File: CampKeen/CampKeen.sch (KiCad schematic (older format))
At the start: 65 parts, among them IC1 LM2597MX-ADJ_NOPB, IC2 LM2670SX-5.0_NOPB, IC3 DS3231SN#, IC4 CD74HC4050ME4, IC5 OPA2340PA, J1 Vin, J2 CircuitSetupsSplitPhase, J3 Vin, J4 Screw_Terminal_01x04, J5 GenEnclosure, J6 GenHeadL, J7 GenHeadR, J8 Conn_01x02, P1 Power, P10 CONN_01X01, P11 CONN_01X01, P12 CONN_01X01, P13 CONN_01X01, P2 Analog, P3 Analog, P4 Digital, P5 PWM, P6 PWM, P7 Communication, P8 CONN_01X01, P9 CONN_01X01, Q40 IRF9Z34NPBF, U2 MAX232

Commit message: updated the pin mapping to the terms. cleaned up the Schematic. PCB placement and routing is what is left to do.
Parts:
- removed J4: Screw_Terminal_01x04, TerminalBlock_TE-Connectivity:TerminalBlock_TE_282834-4_1x04_P2.54mm_Horizontal, symbol Connector:Screw_Terminal_01x04
- added 5VOut1: VS, SamacSys_Parts:BK_HTC-15M, symbol SamacSys_Parts:BK_HTC-15M
- added D3: LED, symbol Device:LED
- added IC6: OPA2340PA, SamacSys_Parts:DIP794W53P254L959H508Q8N, symbol SamacSys_Parts:OPA2340PA
- added J8, J9: Conn_01x02, Connector_PinHeader_2.54mm:PinHeader_1x02_P2.54mm_Vertical, symbol Connector_Generic:Conn_01x02
- added R112, R113: 47K, Resistor_THT:R_Axial_DIN0207_L6.3mm_D2.5mm_P2.54mm_Vertical, symbol Device:R
- added R117: 330, Resistor_THT:R_Axial_DIN0207_L6.3mm_D2.5mm_P2.54mm_Vertical, symbol Device:R
- added RV2, RV3: 500k, Potentiometer_THT:Potentiometer_Bourns_3296W_Vertical, symbol Device:R_POT_US
- IC4: renamed from IC5; footprint DIP794W53P254L959H508Q8N -> SamacSys_Parts:DIP794W53P254L959H508Q8N
- IC5: renamed from IC4; footprint SOIC127P600X175-16N -> SamacSys_Parts:SOIC127P600X175-16N
- IO1: renamed from Tanks0; value Tanks -> IO1
- IO2: renamed from I1; value I1 -> IO2
- IO3: renamed from O1; value O1 -> IO3
- IO4: renamed from IO1; value IO2 -> IO4
- RV1: value R_POT_US -> 500k
- renumbered C7 to C10, C5 to C11, C14 to C12, C15 to C13, C16 to C14, C17 to C15, C9 to C3, C18 to C4, C3 to C5, C8 to C6, C4 to C7, C6 to C8, C10 to C9, J3 to J2, J8 to J3, J2 to J4, L2 to L1, L1 to L2, Q40 to Q1, R6 to R10, R29 to R11, R89 to R5, R28 to R6, R82 to R7, R35 to R8, R5 to R9, U2 to U1
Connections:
- net labels added: AUXVoltage1, AUXVoltage2, AlarmTTL, BRLED, BathRoomTTL, COMRXTTL, COMTXTTL, CWV, DisplayLED, ENLCD, EnCS, IO11, IO110, IO111, IO112, IO12, IO13, IO14, IO15, IO16, IO17, IO18, IO19, IO210, IO211, IO212, IO22, IO23, IO24, IO25, IO26, IO27, IO28, IO29, IO31, IO311, IO32, IO33, IO34, IO35, IO38, IO41, IO410, IO411, IO412, IO42, IO44, IO45, IO47, IO48, IO49, KLED, KitchenTTL, LCBBACK, LCDBL, LCDPOWER, RTankPOWER, RX232, SO1, SO2, SO3, SO4, SO5, SPIn1, SPIn2, SPIn3, SPIn4, SPIn5, SPIn6, SpareTTL, TX232, WLED, WP, WPS, WSS, WSiren
- wire segments 305 -> 447
- no-connect marks 38 -> 39
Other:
- note added: "Energy Monitoring"
- note added: "IO Terminals"
- note added: "Temps: RTD and NTC"
- note removed: "RTD DEV"
- moved on the sheet: C11, C3, C4, C5, C6, C9, D1, IC2, IC3, IC5, IO1, IO2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

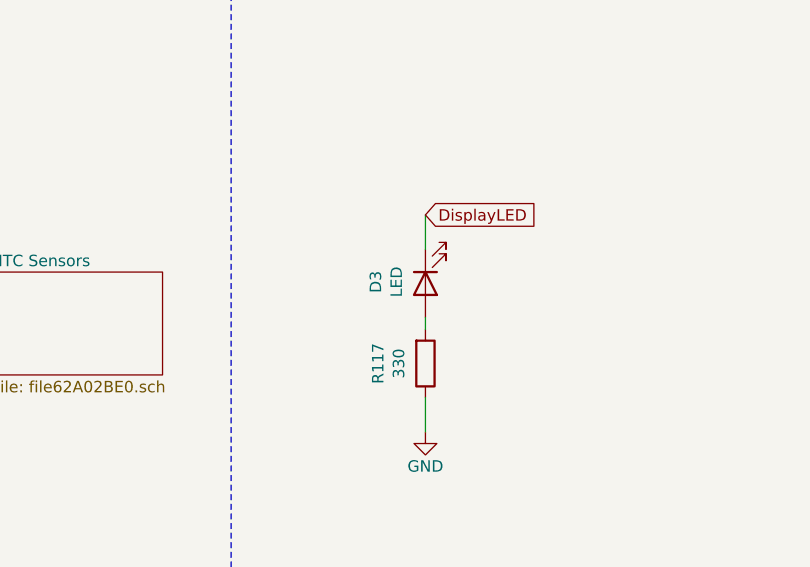
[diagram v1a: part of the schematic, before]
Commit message: fixed the Diode orientation.
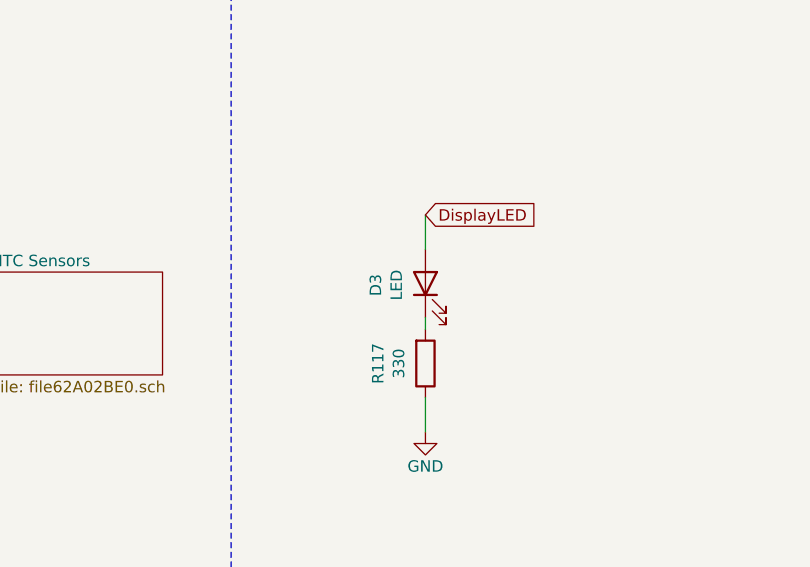
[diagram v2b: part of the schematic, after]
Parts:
- D3: footprint (none) -> LED_THT:LED_D3.0mm
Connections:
- net DisplayLED: now also D3.2 (A); no longer D3.1 (K)
- net at R117.2: now also D3.1 (K); no longer D3.2 (A)
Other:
- moved on the sheet: D3
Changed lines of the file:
@@
 Wire Wire Line
 	17800 2600 17800 2750
-$Comp
-L Device:LED D3
-U 1 1 648097C3
-P 17800 2100
-F 0 "D3" H 17793 2317 50  0000 C CNN
-F 1 "LED" H 17793 2226 50  0000 C CNN
-F 2 "" H 17800 2100 50  0001 C CNN
-F 3 "~" H 17800 2100 50  0001 C CNN
-	1    17800 2100
-	0    -1   1    0
-$EndComp
 Wire Wire Line
 	17800 2300 17800 2250
-Wire Wire Line
-	17800 1950 17800 1800
 NoConn ~ 21800 1300
 NoConn ~ 21800 1200
@@
 Wire Wire Line
 	6900 7750 7450 7750
+Wire Wire Line
+	17800 1950 17800 1800
+$Comp
+L Device:LED D3
+U 1 1 648097C3
+P 17800 2100
+F 0 "D3" H 17793 2317 50  0000 C CNN
+F 1 "LED" H 17793 2226 50  0000 C CNN
+F 2 "LED_THT:LED_D3.0mm" H 17800 2100 50  0001 C CNN
+F 3 "~" H 17800 2100 50  0001 C CNN
+	1    17800 2100
+	0    -1   -1   0
+$EndComp
 $EndSCHEMATC

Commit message: separated the 12 and 5 volt outputs. added another spare output.
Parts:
- removed J2: Vin, TerminalBlock_Phoenix:TerminalBlock_Phoenix_MKDS-1,5-2-5.08_1x02_P5.08mm_Horizontal, symbol Connector:Screw_Terminal_01x02
- added J2: Screw_Terminal_01x03, TerminalBlock_Phoenix:TerminalBlock_Phoenix_MKDS-1,5-3-5.08_1x03_P5.08mm_Horizontal, symbol Connector:Screw_Terminal_01x03
- renumbered C9 to C10, C10 to C11, C11 to C3, C3 to C4, C4 to C5, C5 to C6, C6 to C7, C7 to C8, C8 to C9, IC5 to IC1, IC1 to IC2, IC2 to IC3, IC3 to IC4, IC4 to IC5, J4 to J3, J8 to J4, J3 to J5, J9 to J6, J5 to J7, J6 to J8, J7 to J9, R8 to R10, R112 to R11, R11 to R12, R113 to R13, R117 to R14, R9 to R6, R10 to R7, R6 to R8, R7 to R9, RV2 to RV1, RV1 to RV2
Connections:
- net +12V: now also J2.1 (Pin_1)
- net GND: now also J2.2 (Pin_2)
- net 15(Rx3) renamed SO6
- new net SpareOut6: J2.3 (Pin_3)
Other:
- note added: "Inputs"
- note added: "Outputs"
- note added: "Tank Sensors"
- moved on the sheet: D3, R14

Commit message: fixing the powered 12v out and moving it on the other side of the reverse polarity protection for everything else. Added a Reverse polarity protection diode (3A Schottkey). Also this is still behind the main protection fuse.
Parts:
- added D4: SR305-TP, DIOAD2860W130L840D505, symbol SamacSys_Parts:SR305-TP
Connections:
- net +12V: no longer J2.1 (Pin_1)
- net at Main1.2, Q1.2: now also D4.1
- new net: D4.2, J2.1 (Pin_1)
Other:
- moved on the sheet: D3, J2, R14
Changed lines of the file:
@@
 Text Label 21800 1400 0    60   ~ 0
 AREF
-Text Notes 20075 575  0    60   ~ 0
+Text Notes 19225 575  0    60   ~ 0
 Shield for Arduino Mega Rev 3
 Text Notes 22400 1000 0    60   ~ 0
@@
 	22900 1000 22150 1000
 Wire Notes Line
-	21550 650  21550 475
+	20700 650  20700 475
 Wire Notes Line
-	20050 650  21550 650
+	19200 650  20700 650
 Wire Wire Line
 	20400 1100 20400 1800
@@
 $EndComp
 Wire Wire Line
-	3450 1100 3200 1100
-Wire Wire Line
 	4050 1100 4750 1100
 $Comp
@@
 Wire Wire Line
 	4750 1100 4750 1050
-Wire Wire Line
-	2400 1100 1650 1100
 Connection ~ 2400 1100
 $Comp
@@
 	900  10200 900  11000
 Wire Wire Line
-	4600 1200 4600 1250
+	4350 2500 4350 2550
 Wire Wire Line
-	4750 1200 4600 1200
+	4500 2500 4350 2500
 $Comp
 L power:GND #PWR027
 U 1 1 61491D30
-P 4600 1250
-F 0 "#PWR027" H 4600 1000 50  0001 C CNN
-F 1 "GND" H 4605 1077 50  0000 C CNN
-F 2 "" H 4600 1250 50  0001 C CNN
-F 3 "" H 4600 1250 50  0001 C CNN
-	1    4600 1250
+P 4350 2550
+F 0 "#PWR027" H 4350 2300 50  0001 C CNN
+F 1 "GND" H 4355 2377 50  0000 C CNN
+F 2 "" H 4350 2550 50  0001 C CNN
+F 3 "" H 4350 2550 50  0001 C CNN
+	1    4350 2550
 	1    0    0    -1
 $EndComp
@@
 Wire Wire Line
 	21550 1600 22200 1600
-Text GLabel 17900 1550 2    50   Input ~ 0
+Text GLabel 18000 750  2    50   Input ~ 0
 DisplayLED
 $Comp
 L Device:R R14
 U 1 1 647E4AAA
-P 17900 2200
-F 0 "R14" V 17693 2200 50  0000 C CNN
-F 1 "330" V 17784 2200 50  0000 C CNN
-F 2 "Resistor_THT:R_Axial_DIN0207_L6.3mm_D2.5mm_P2.54mm_Vertical" V 17830 2200 50  0001 C CNN
-F 3 "~" H 17900 2200 50  0001 C CNN
-	1    17900 2200
+P 18000 1400
+F 0 "R14" V 17793 1400 50  0000 C CNN
+F 1 "330" V 17884 1400 50  0000 C CNN
+F 2 "Resistor_THT:R_Axial_DIN0207_L6.3mm_D2.5mm_P2.54mm_Vertical" V 17930 1400 50  0001 C CNN
+F 3 "~" H 18000 1400 50  0001 C CNN
+	1    18000 1400
 	1    0    0    1
 $EndComp
@@
 L power:GND #PWR056
 U 1 1 647E4AB0
-P 17900 2500
-F 0 "#PWR056" H 17900 2250 50  0001 C CNN
-F 1 "GND" H 17900 2350 50  0000 C CNN
-F 2 "" H 17900 2500 50  0000 C CNN
-F 3 "" H 17900 2500 50  0000 C CNN
-	1    17900 2500
+P 18000 1700
+F 0 "#PWR056" H 18000 1450 50  0001 C CNN
+F 1 "GND" H 18000 1550 50  0000 C CNN
+F 2 "" H 18000 1700 50  0000 C CNN
+F 3 "" H 18000 1700 50  0000 C CNN
+	1    18000 1700
 	-1   0    0    -1
 $EndComp
 Wire Wire Line
-	17900 2350 17900 2500
+	18000 1550 18000 1700
 Wire Wire Line
-	17900 2050 17900 2000
+	18000 1250 18000 1200
 NoConn ~ 21800 1300
 NoConn ~ 21800 1200
@@
 	6900 7750 7450 7750
 Wire Wire Line
-	17900 1700 17900 1550
+	18000 900  18000 750
 $Comp
 L Device:LED D3
 U 1 1 648097C3
-P 17900 1850
-F 0 "D3" H 17893 2067 50  0000 C CNN
-F 1 "LED" H 17893 1976 50  0000 C CNN
-F 2 "LED_THT:LED_D3.0mm" H 17900 1850 50  0001 C CNN
-F 3 "~" H 17900 1850 50  0001 C CNN
-	1    17900 1850
+P 18000 1050
+F 0 "D3" H 17993 1267 50  0000 C CNN
+F 1 "LED" H 17993 1176 50  0000 C CNN
+F 2 "LED_THT:LED_D3.0mm" H 18000 1050 50  0001 C CNN
+F 3 "~" H 18000 1050 50  0001 C CNN
+	1    18000 1050
 	0    -1   -1   0
 $EndComp
@@
 L Connector:Screw_Terminal_01x03 J2
 U 1 1 61F0BAC6
-P 4950 1200
-F 0 "J2" H 5030 1242 50  0000 L CNN
-F 1 "Screw_Terminal_01x03" H 5030 1151 50  0000 L CNN
-F 2 "TerminalBlock_Phoenix:TerminalBlock_Phoenix_MKDS-1,5-3-5.08_1x03_P5.08mm_Horizontal" H 4950 1200 50  0001 C CNN
-F 3 "~" H 4950 1200 50  0001 C CNN
-	1    4950 1200
+P 4700 2500
+F 0 "J2" H 4780 2542 50  0000 L CNN
+F 1 "Screw_Terminal_01x03" H 4780 2451 50  0000 L CNN
+F 2 "TerminalBlock_Phoenix:TerminalBlock_Phoenix_MKDS-1,5-3-5.08_1x03_P5.08mm_Horizontal" H 4700 2500 50  0001 C CNN
+F 3 "~" H 4700 2500 50  0001 C CNN
+	1    4700 2500
 	1    0    0    -1
 $EndComp
-Connection ~ 4750 1100
 Wire Wire Line
 	12700 10200 12550 10200
@@
 Wire Wire Line
 	10500 10200 10650 10200
-Text GLabel 4750 1550 0    50   Input ~ 0
+Text GLabel 4500 2850 0    50   Input ~ 0
 SpareOut6
 Wire Wire Line
-	4750 1550 4750 1300
+	4500 2850 4500 2600
 Text Notes 10400 7050 0    197  ~ 0
 Tank Sensors
@@
 Wire Notes Line
 	9850 7200 16950 7200
+Wire Wire Line
+	2400 1100 1650 1100
+Wire Wire Line
+	3200 1100 3350 1100
+$Comp
+L SamacSys_Parts:SR305-TP D4
+U 1 1 61BA258E
+P 3700 2400
+F 0 "D4" H 4100 2667 50  0000 C CNN
+F 1 "SR305-TP" H 4100 2576 50  0000 C CNN
+F 2 "DIOAD2860W130L840D505" H 4200 2550 50  0001 L CNN
+F 3 "https://componentsearchengine.com/Datasheets/1/SR305-TP.pdf" H 4200 2450 50  0001 L CNN
+F 4 "Schottky Diodes & Rectifiers Rectifier 50V 80A" H 4200 2350 50  0001 L CNN "Description"
+F 5 "" H 4200 2250 50  0001 L CNN "Height"
+F 6 "833-SR305-TP" H 4200 2150 50  0001 L CNN "Mouser Part Number"
+F 7 "https://www.mouser.com/Search/Refine.aspx?Keyword=833-SR305-TP" H 4200 2050 50  0001 L CNN "Mouser Price/Stock"
+F 8 "Micro Commercial Components (MCC)" H 4200 1950 50  0001 L CNN "Manufacturer_Name"
+F 9 "SR305-TP" H 4200 1850 50  0001 L CNN "Manufacturer_Part_Number"
+	1    3700 2400
+	1    0    0    -1
+$EndComp
+Wire Wire Line
+	4400 2400 4500 2400
+Wire Wire Line
+	3800 2400 3350 2400
+Wire Wire Line
+	3350 2400 3350 1100
+Connection ~ 3350 1100
+Wire Wire Line
+	3350 1100 3450 1100
+Wire Notes Line
+	19200 500  19200 6500
+Wire Notes Line
+	19200 6500 22900 6500
+Wire Notes Line
+	16950 2250 19200 2250
 $EndSCHEMATC

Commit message: some annotation.
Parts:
- removed D3: LED, LED_THT:LED_D3.0mm, symbol Device:LED
- removed R14: 330, Resistor_THT:R_Axial_DIN0207_L6.3mm_D2.5mm_P2.54mm_Vertical, symbol Device:R
- added D5: SR305-TP, DIOAD2860W130L840D505, symbol SamacSys_Parts:SR305-TP
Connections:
- net +5V: now also 5VOut1.2, IO2.1, D5.2; no longer 5VOut1.1, C10.1, IC3.6 (FEEDBACK/FB), L1.2
- net at Main1.2, Q1.2: now also D4.2; no longer D4.1
- net at J2.1 (Pin_1): now also D4.1; no longer D4.2
- net DisplayLED renamed 13(**)
- new net: 5VOut1.1, C10.1, IC3.6 (FEEDBACK/FB), L1.2
- new net +5VL: D5.1
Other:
- note added: "5V - Clean Voltage Line\n5VL - Dirty Logic line for external interfacing"
- moved on the sheet: 5VOut1
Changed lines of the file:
@@
 Connection ~ 4400 6300
 Wire Wire Line
-	4400 5900 4400 6300
+	5050 5900 5050 6300
 Wire Wire Line
 	3350 6800 3500 6800
@@
 L power:+5V #PWR023
 U 1 1 65AC81D1
-P 4400 5900
-F 0 "#PWR023" H 4400 5750 50  0001 C CNN
-F 1 "+5V" H 4415 6073 50  0000 C CNN
-F 2 "" H 4400 5900 50  0001 C CNN
-F 3 "" H 4400 5900 50  0001 C CNN
-	1    4400 5900
+P 5050 5900
+F 0 "#PWR023" H 5050 5750 50  0001 C CNN
+F 1 "+5V" H 5065 6073 50  0000 C CNN
+F 2 "" H 5050 5900 50  0001 C CNN
+F 3 "" H 5050 5900 50  0001 C CNN
+	1    5050 5900
 	1    0    0    -1
 $EndComp
@@
 	1    0    0    -1
 $EndComp
-$Comp
-L power:GND #PWR014
-U 1 1 69EC12CF
-P 3650 2000
-F 0 "#PWR014" H 3650 1750 50  0001 C CNN
-F 1 "GND" H 3655 1827 50  0000 C CNN
-F 2 "" H 3650 2000 50  0001 C CNN
-F 3 "" H 3650 2000 50  0001 C CNN
-	1    3650 2000
-	-1   0    0    -1
-$EndComp
-Wire Wire Line
-	3650 2000 3650 1900
 Wire Wire Line
 	3650 1600 3650 1400
@@
 F13 "SPOut6" I L 10650 10200 50
 $EndSheet
-Text GLabel 22200 1600 2    50   Input ~ 0
-DisplayLED
 Wire Wire Line
 	21550 1600 22200 1600
-Text GLabel 18000 750  2    50   Input ~ 0
-DisplayLED
-$Comp
-L Device:R R14
-U 1 1 647E4AAA
-P 18000 1400
-F 0 "R14" V 17793 1400 50  0000 C CNN
-F 1 "330" V 17884 1400 50  0000 C CNN
-F 2 "Resistor_THT:R_Axial_DIN0207_L6.3mm_D2.5mm_P2.54mm_Vertical" V 17930 1400 50  0001 C CNN
-F 3 "~" H 18000 1400 50  0001 C CNN
-	1    18000 1400
-	1    0    0    1
-$EndComp
-$Comp
-L power:GND #PWR056
-U 1 1 647E4AB0
-P 18000 1700
-F 0 "#PWR056" H 18000 1450 50  0001 C CNN
-F 1 "GND" H 18000 1550 50  0000 C CNN
-F 2 "" H 18000 1700 50  0000 C CNN
-F 3 "" H 18000 1700 50  0000 C CNN
-	1    18000 1700
-	-1   0    0    -1
-$EndComp
-Wire Wire Line
-	18000 1550 18000 1700
-Wire Wire Line
-	18000 1250 18000 1200
 NoConn ~ 21800 1300
 NoConn ~ 21800 1200
@@
 Text GLabel 8450 8900 2    50   Input ~ 0
 AUXVoltage1
-Wire Wire Line
-	6800 7700 6800 7750
 $Comp
 L SamacSys_Parts:1727751 IO4
@@
 L SamacSys_Parts:BK_HTC-15M 5VOut1
 U 1 1 63086201
-P 6800 7750
-F 0 "5VOut1" H 7428 7746 50  0000 L CNN
-F 1 "VS" H 7428 7655 50  0000 L CNN
-F 2 "SamacSys_Parts:BK_HTC-15M" H 7450 7850 50  0001 L CNN
-F 3 "" H 7450 7750 50  0001 L CNN
-F 4 "Fuse Holder PCB FUSE BLOCK" H 7450 7650 50  0001 L CNN "Description"
-F 5 "" H 7450 7550 50  0001 L CNN "Height"
-F 6 "504-HTC-15M" H 7450 7450 50  0001 L CNN "Mouser Part Number"
-F 7 "https://www.mouser.co.uk/ProductDetail/Bussmann-Eaton/BK-HTC-15M?qs=xYgILgh9YcIcij8kQUilpQ%3D%3D" H 7450 7350 50  0001 L CNN "Mouser Price/Stock"
-F 8 "Eaton" H 7450 7250 50  0001 L CNN "Manufacturer_Name"
-F 9 "BK/HTC-15M" H 7450 7150 50  0001 L CNN "Manufacturer_Part_Number"
-	1    6800 7750
+P 4600 6300
+F 0 "5VOut1" H 5228 6296 50  0000 L CNN
+F 1 "VS" H 5228 6205 50  0000 L CNN
+F 2 "SamacSys_Parts:BK_HTC-15M" H 5250 6400 50  0001 L CNN
+F 3 "" H 5250 6300 50  0001 L CNN
+F 4 "Fuse Holder PCB FUSE BLOCK" H 5250 6200 50  0001 L CNN "Description"
+F 5 "" H 5250 6100 50  0001 L CNN "Height"
+F 6 "504-HTC-15M" H 5250 6000 50  0001 L CNN "Mouser Part Number"
+F 7 "https://www.mouser.co.uk/ProductDetail/Bussmann-Eaton/BK-HTC-15M?qs=xYgILgh9YcIcij8kQUilpQ%3D%3D" H 5250 5900 50  0001 L CNN "Mouser Price/Stock"
+F 8 "Eaton" H 5250 5800 50  0001 L CNN "Manufacturer_Name"
+F 9 "BK/HTC-15M" H 5250 5700 50  0001 L CNN "Manufacturer_Part_Number"
+	1    4600 6300
 	0    -1   1    0
 $EndComp
@@
 L power:+5V #PWR034
 U 1 1 6265DF69
-P 6800 7700
-F 0 "#PWR034" H 6800 7550 50  0001 C CNN
-F 1 "+5V" H 6815 7873 50  0000 C CNN
-F 2 "" H 6800 7700 50  0001 C CNN
-F 3 "" H 6800 7700 50  0001 C CNN
-	1    6800 7700
+P 7250 7750
+F 0 "#PWR034" H 7250 7600 50  0001 C CNN
+F 1 "+5V" H 7265 7923 50  0000 C CNN
+F 2 "" H 7250 7750 50  0001 C CNN
+F 3 "" H 7250 7750 50  0001 C CNN
+	1    7250 7750
 	-1   0    0    -1
 $EndComp
@@
 Wire Wire Line
 	14150 5700 14300 5700
-Wire Wire Line
-	6900 7750 7450 7750
-Wire Wire Line
-	18000 900  18000 750
-$Comp
-L Device:LED D3
-U 1 1 648097C3
-P 18000 1050
-F 0 "D3" H 17993 1267 50  0000 C CNN
-F 1 "LED" H 17993 1176 50  0000 C CNN
-F 2 "LED_THT:LED_D3.0mm" H 18000 1050 50  0001 C CNN
-F 3 "~" H 18000 1050 50  0001 C CNN
-	1    18000 1050
-	0    -1   -1   0
-$EndComp
 $Sheet
 S 10650 9050 1900 300
@@
 Wire Wire Line
 	3200 1100 3350 1100
-$Comp
-L SamacSys_Parts:SR305-TP D4
-U 1 1 61BA258E
-P 3700 2400
-F 0 "D4" H 4100 2667 50  0000 C CNN
-F 1 "SR305-TP" H 4100 2576 50  0000 C CNN
-F 2 "DIOAD2860W130L840D505" H 4200 2550 50  0001 L CNN
-F 3 "https://componentsearchengine.com/Datasheets/1/SR305-TP.pdf" H 4200 2450 50  0001 L CNN
-F 4 "Schottky Diodes & Rectifiers Rectifier 50V 80A" H 4200 2350 50  0001 L CNN "Description"
-F 5 "" H 4200 2250 50  0001 L CNN "Height"
-F 6 "833-SR305-TP" H 4200 2150 50  0001 L CNN "Mouser Part Number"
-F 7 "https://www.mouser.com/Search/Refine.aspx?Keyword=833-SR305-TP" H 4200 2050 50  0001 L CNN "Mouser Price/Stock"
-F 8 "Micro Commercial Components (MCC)" H 4200 1950 50  0001 L CNN "Manufacturer_Name"
-F 9 "SR305-TP" H 4200 1850 50  0001 L CNN "Manufacturer_Part_Number"
-	1    3700 2400
-	1    0    0    -1
-$EndComp
 Wire Wire Line
 	4400 2400 4500 2400
@@
 Wire Notes Line
 	16950 2250 19200 2250
+Wire Wire Line
+	3650 2000 3650 1900
+$Comp
+L power:GND #PWR014
+U 1 1 69EC12CF
+P 3650 2000
+F 0 "#PWR014" H 3650 1750 50  0001 C CNN
+F 1 "GND" H 3655 1827 50  0000 C CNN
+F 2 "" H 3650 2000 50  0001 C CNN
+F 3 "" H 3650 2000 50  0001 C CNN
+	1    3650 2000
+	-1   0    0    -1
+$EndComp
+$Comp
+L SamacSys_Parts:SR305-TP D4
+U 1 1 61BA258E
+P 4500 2400
+F 0 "D4" H 4900 2667 50  0000 C CNN
+F 1 "SR305-TP" H 4900 2576 50  0000 C CNN
+F 2 "DIOAD2860W130L840D505" H 5000 2550 50  0001 L CNN
+F 3 "https://componentsearchengine.com/Datasheets/1/SR305-TP.pdf" H 5000 2450 50  0001 L CNN
+F 4 "Schottky Diodes & Rectifiers Rectifier 50V 80A" H 5000 2350 50  0001 L CNN "Description"
+F 5 "" H 5000 2250 50  0001 L CNN "Height"
+F 6 "833-SR305-TP" H 5000 2150 50  0001 L CNN "Mouser Part Number"
+F 7 "https://www.mouser.com/Search/Refine.aspx?Keyword=833-SR305-TP" H 5000 2050 50  0001 L CNN "Mouser Price/Stock"
+F 8 "Micro Commercial Components (MCC)" H 5000 1950 50  0001 L CNN "Manufacturer_Name"
+F 9 "SR305-TP" H 5000 1850 50  0001 L CNN "Manufacturer_Part_Number"
+	1    4500 2400
+	-1   0    0    -1
+$EndComp
+$Comp
+L power:+5VL #PWR097
+U 1 1 61AB0C18
+P 5800 5900
+F 0 "#PWR097" H 5800 5750 50  0001 C CNN
+F 1 "+5VL" H 5815 6073 50  0000 C CNN
+F 2 "" H 5800 5900 50  0001 C CNN
+F 3 "" H 5800 5900 50  0001 C CNN
+	1    5800 5900
+	1    0    0    -1
+$EndComp
+$Comp
+L SamacSys_Parts:SR305-TP D5
+U 1 1 61AB378D
+P 5750 6300
+F 0 "D5" H 6150 6567 50  0000 C CNN
+F 1 "SR305-TP" H 6150 6476 50  0000 C CNN
+F 2 "DIOAD2860W130L840D505" H 6250 6450 50  0001 L CNN
+F 3 "https://componentsearchengine.com/Datasheets/1/SR305-TP.pdf" H 6250 6350 50  0001 L CNN
+F 4 "Schottky Diodes & Rectifiers Rectifier 50V 80A" H 6250 6250 50  0001 L CNN "Description"
+F 5 "" H 6250 6150 50  0001 L CNN "Height"
+F 6 "833-SR305-TP" H 6250 6050 50  0001 L CNN "Mouser Part Number"
+F 7 "https://www.mouser.com/Search/Refine.aspx?Keyword=833-SR305-TP" H 6250 5950 50  0001 L CNN "Mouser Price/Stock"
+F 8 "Micro Commercial Components (MCC)" H 6250 5850 50  0001 L CNN "Manufacturer_Name"
+F 9 "SR305-TP" H 6250 5750 50  0001 L CNN "Manufacturer_Part_Number"
+	1    5750 6300
+	-1   0    0    -1
+$EndComp
+Wire Wire Line
+	5650 6300 5800 6300
+Wire Wire Line
+	5800 6300 5800 5900
+Wire Wire Line
+	7250 7750 7450 7750
+Wire Wire Line
+	4400 6300 4600 6300
+Wire Wire Line
+	4700 6300 5050 6300
+Connection ~ 5050 6300
+Text Notes 4150 5650 0    50   ~ 0
+5V - Clean Voltage Line\n5VL - Dirty Logic line for external interfacing
 $EndSCHEMATC

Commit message: wip for working on the input circuits on the board. they are getting upgraded with opto-isolation as i've found that you can burn out the processor board if there is a voltage applied to an input when the system is on and then turned off. for the code fixing some of the LCD display code.
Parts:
- removed D5: SR305-TP, DIOAD2860W130L840D505, symbol SamacSys_Parts:SR305-TP
- added IC10, IC7, IC8, IC9: SN7404DR, SOIC127P600X175-14N, symbol SamacSys_Parts:SN7404DR
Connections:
- net +5V: now also IC10.14 (VCC), IC7.14 (VCC), IC8.14 (VCC), IC9.14 (VCC)
- net AlarmTTL: now also IC7.2 (1Y)
- net BathRoomTTL: now also IC7.6 (3Y)
- net ENLCD: now also IC7.8 (4Y)
- net G1-2: now also IC10.4 (2Y)
- net G1-4: now also IC10.2 (1Y)
- net G3-4: now also IC10.6 (3Y)
- net G4-4: now also IC10.8 (4Y)
- net GND: now also IC10.7 (GND), IC7.7 (GND), IC8.7 (GND), IC9.7 (GND)
- net KitchenTTL: now also IC7.4 (2Y)
- net LCBBACK: now also IC8.2 (1Y)
- net S1-2: now also IC9.4 (2Y)
- net S1-4: now also IC9.2 (1Y)
- net S3-4: now also IC9.6 (3Y)
- net S4-4: now also IC9.8 (4Y)
- net SPIn1: now also IC8.6 (3Y)
- net SPIn2: now also IC8.12 (6Y)
- net SPIn3: now also IC8.10 (5Y)
- net SPIn4: now also IC8.8 (4Y)
- net SPIn5: now also IC9.12 (6Y)
- net SPIn6: now also IC9.10 (5Y)
- net SpareTTL: now also IC7.12 (6Y)
- net WPS: now also IC7.10 (5Y)
- net WSS: now also IC8.4 (2Y)
- new net Inputs With Interrupts/AlarmResetTTL: IC7.1 (1A)
- new net Inputs With Interrupts/BathroomTTL: IC7.5 (3A)
- new net Inputs With Interrupts/KitchenTTL: IC7.3 (2A)
- new net Inputs With Interrupts/SpareInterruptTTL: IC7.13 (6A)
- new net Inputs/EnableLCDTTL: IC7.9 (4A)
- new net Inputs/LCDBackLIGHTTTL: IC8.1 (1A)
- new net Inputs/SP1TTL: IC8.5 (3A)
- new net Inputs/SP2TTL: IC8.13 (6A)
- new net Inputs/SP3TTL: IC8.11 (5A)
- new net Inputs/SP4TTL: IC8.9 (4A)
- new net Inputs/SP5TTL: IC9.13 (6A)
- new net Inputs/SP6TTL: IC9.11 (5A)
- new net Inputs/WaterPumpSenseTTL: IC7.11 (5A)
- new net Inputs/WaterSourceTTL: IC8.3 (2A)
- new net Tanks/1-2OUT: IC9.3 (2A)
- new net Tanks/1-4OUT: IC9.1 (1A)
- new net Tanks/3-4OUT: IC9.5 (3A)
- new net Tanks/FullOUT: IC9.9 (4A)
- new net sheet6479D10C/1-2OUT: IC10.3 (2A)
- new net sheet6479D10C/1-4OUT: IC10.1 (1A)
- new net sheet6479D10C/3-4OUT: IC10.5 (3A)
- new net sheet6479D10C/FullOUT: IC10.9 (4A)
- no-connect marks 39 -> 43
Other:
- note removed: "5V - Clean Voltage Line\n5VL - Dirty Logic line for external interfacing"
- moved on the sheet: RTCBattery1
